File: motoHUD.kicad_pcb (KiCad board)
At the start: 2 copper layers, 128 x 55 mm, 90 parts, among them J1 POWER, J10 LCD Connector, J2 SIGNAL, J3 THERM1, J4 THERM2, J5 HALL, J6 SIG_RPM, J8 USB_B_Mini, J9 STLink, M1 X27 168, Q1 2N7002KQ-13, Q2 2N7002KQ-13, U1 AZ1117-3.3, U2 AZ1117-5.0, U3 LM2903DT, U4 STM32F103C8Tx, U5 M95320-WMN6P, Y1 8M, Y2 32,768k

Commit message: schematic rev2
2nd revision schematic and updated BOM
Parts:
- J10: footprint motoHUD:ILI9341 FFC -> motoHUD:ILI9341FFC
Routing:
- net Net-(J2-Pad2): track 7.66 -> 8.49 mm

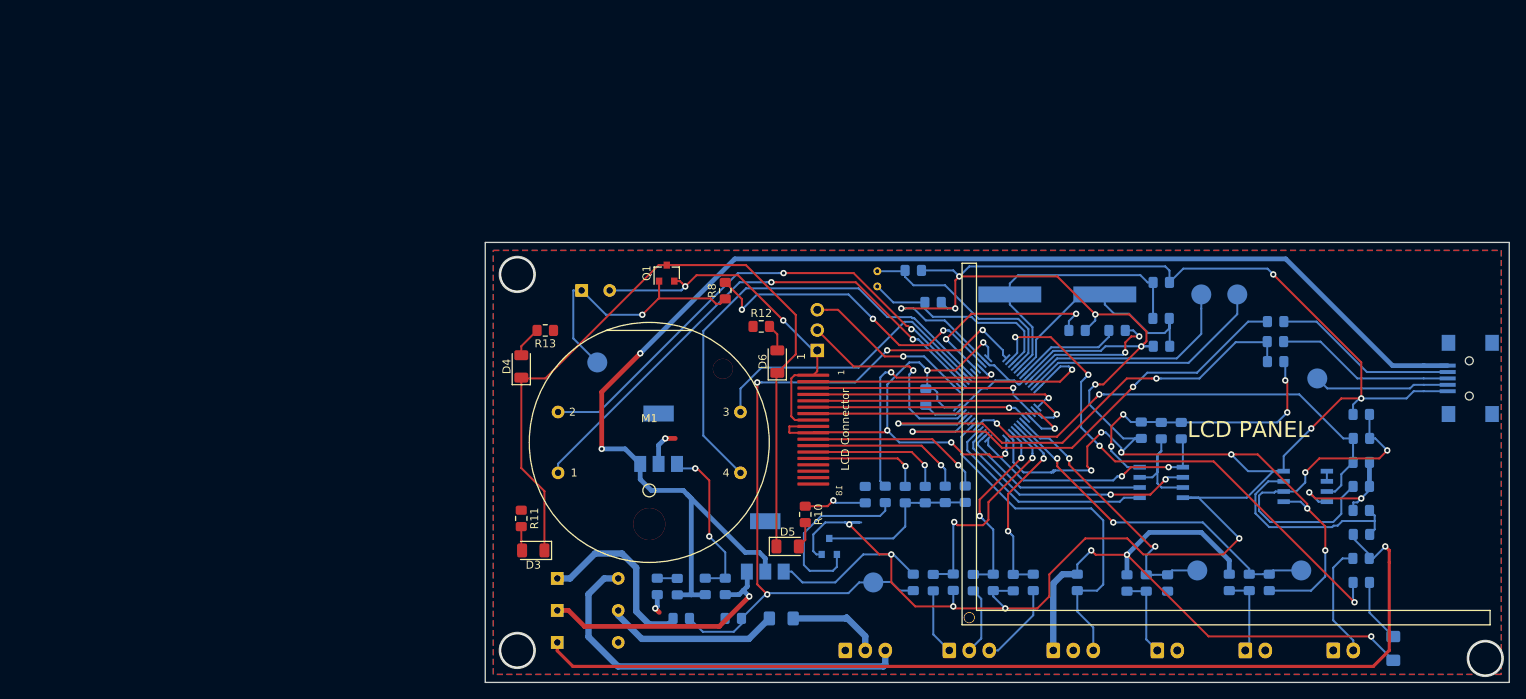
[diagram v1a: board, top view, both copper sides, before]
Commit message: new netlist imported to board design
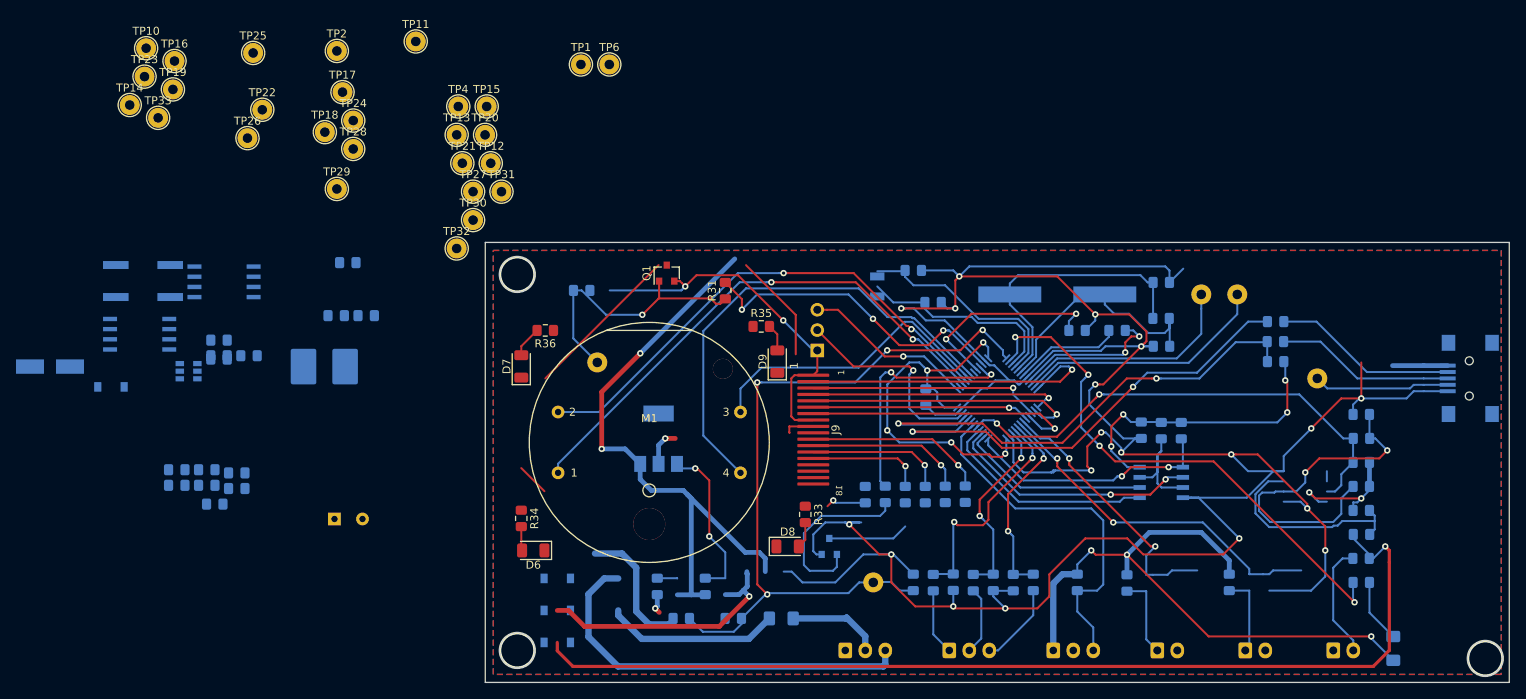
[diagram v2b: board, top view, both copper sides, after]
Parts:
- removed C2: 10u, Capacitor_SMD:C_0805_2012Metric_Pad1.15x1.40mm_HandSolder
- removed C3, C4: 2,2u, Capacitor_SMD:C_0805_2012Metric_Pad1.15x1.40mm_HandSolder
- removed C7: 22u, Capacitor_SMD:C_0805_2012Metric_Pad1.15x1.40mm_HandSolder
- removed C8: 100u, Capacitor_THT:CP_Radial_D8.0mm_P3.50mm
- removed the D8 at (85.0, 131.0)
- removed J10: LCD Connector, motoHUD:ILI9341FFC
- removed R4, R5: 100K, Resistor_SMD:R_0805_2012Metric_Pad1.15x1.40mm_HandSolder
- removed REF**: KiCAD Logo, Symbol:Symbol_KiCAD-Logo_CopperAndSilkScreenTop
- added C12: 10u 16v, Capacitor_SMD:C_0805_2012Metric_Pad1.15x1.40mm_HandSolder, B.Cu at (58.8, 83.5)
- added C13: 0,1u, Capacitor_SMD:C_0805_2012Metric_Pad1.15x1.40mm_HandSolder, B.Cu at (41.2, 111.4)
- added C14: 10u 16v, Capacitor_SMD:C_0805_2012Metric_Pad1.15x1.40mm_HandSolder, B.Cu at (37.4, 109.4)
- added C15: 10u 16v, Capacitor_SMD:C_0805_2012Metric_Pad1.15x1.40mm_HandSolder, B.Cu at (37.4, 111.4)
- added C16: 100u, Capacitor_THT:CP_Radial_D8.0mm_P3.50mm, B.Cu at (57.1, 115.6)
- added C21: 22u, Capacitor_SMD:C_0805_2012Metric_Pad1.15x1.40mm_HandSolder, B.Cu at (88.0, 87.0)
- added C22: 22u, Capacitor_SMD:C_0805_2012Metric_Pad1.15x1.40mm_HandSolder, B.Cu at (57.4, 90.2)
- added C25: 22u, Capacitor_SMD:C_0805_2012Metric_Pad1.15x1.40mm_HandSolder, B.Cu at (44.9, 111.8)
- added D3: 1N4148W-7-F, Diode_SMD:D_SOD-123, B.Cu at (85.0, 131.0)
- added D4: STPS1L40A, Diode_SMD:D_SMA_Handsoldering, B.Cu at (21.6, 96.5)
- added D5: 1N4148W-7-F, Diode_SMD:D_SOD-123, B.Cu at (29.2, 99.1)
- added J9: LCD Connector, motoHUD:ILI9341 FFC, F.Cu at (117.0, 104.4)
- added L1: DLG-0403-220, Inductor_SMD:L_2816_7142Metric_Pad3.20x4.45mm_HandSolder, B.Cu at (55.9, 96.5)
- added R13: 51,1k, Resistor_SMD:R_0805_2012Metric_Pad1.15x1.40mm_HandSolder, B.Cu at (42.7, 95.2)
- added R14: 1,5k, Resistor_SMD:R_0805_2012Metric_Pad1.15x1.40mm_HandSolder, B.Cu at (42.2, 113.7)
- added R15: 10k, Resistor_SMD:R_0805_2012Metric_Pad1.15x1.40mm_HandSolder, B.Cu at (42.7, 93.2)
- added R16: 0R, Resistor_SMD:R_0805_2012Metric_Pad1.15x1.40mm_HandSolder, B.Cu at (41.2, 109.4)
- added R17: 0R, Resistor_SMD:R_0805_2012Metric_Pad1.15x1.40mm_HandSolder, B.Cu at (42.7, 95.6)
- added R26: 2,2k, Resistor_SMD:R_0805_2012Metric_Pad1.15x1.40mm_HandSolder, B.Cu at (46.5, 95.2)
- added R32: 0R, Resistor_SMD:R_0805_2012Metric_Pad1.15x1.40mm_HandSolder, B.Cu at (44.9, 109.8)
- added R62: 0R, Resistor_SMD:R_0805_2012Metric_Pad1.15x1.40mm_HandSolder, B.Cu at (61.1, 90.2)
- added SW1: TACTM-613N-F, Button_Switch_SMD:SW_SPST_EVQQ2, B.Cu at (33.2, 85.8)
- added TP10: TEMP1, TestPoint:TestPoint_THTPad_D2.5mm_Drill1.2mm, F.Cu at (33.6, 56.7)
- added TP11: TEMP2, TestPoint:TestPoint_THTPad_D2.5mm_Drill1.2mm, F.Cu at (67.3, 55.9)
- added TP12: RPMA, TestPoint:TestPoint_THTPad_D2.5mm_Drill1.2mm, F.Cu at (76.7, 71.1)
- added TP13: BOOST, TestPoint:TestPoint_THTPad_D2.5mm_Drill1.2mm, F.Cu at (72.4, 67.6)
- added TP14: BCKL_V, TestPoint:TestPoint_THTPad_D2.5mm_Drill1.2mm, F.Cu at (31.6, 63.8)
- added TP15: RPMC, TestPoint:TestPoint_THTPad_D2.5mm_Drill1.2mm, F.Cu at (76.2, 64.0)
- added TP16: RPMD, TestPoint:TestPoint_THTPad_D2.5mm_Drill1.2mm, F.Cu at (37.2, 58.3)
- added TP17: BLINK, TestPoint:TestPoint_THTPad_D2.5mm_Drill1.2mm, F.Cu at (58.2, 62.2)
- added TP18: BLINK12, TestPoint:TestPoint_THTPad_D2.5mm_Drill1.2mm, F.Cu at (55.9, 67.2)
- added TP19: HIBEAM, TestPoint:TestPoint_THTPad_D2.5mm_Drill1.2mm, F.Cu at (37.0, 61.9)
- added TP20: HIBEAM12, TestPoint:TestPoint_THTPad_D2.5mm_Drill1.2mm, F.Cu at (76.0, 67.6)
- added TP21: NTR, TestPoint:TestPoint_THTPad_D2.5mm_Drill1.2mm, F.Cu at (73.1, 71.1)
- added TP22: NTR12, TestPoint:TestPoint_THTPad_D2.5mm_Drill1.2mm, F.Cu at (48.1, 64.4)
- added TP23: CS2, TestPoint:TestPoint_THTPad_D2.5mm_Drill1.2mm, F.Cu at (33.4, 60.3)
- added TP24: SCK1, TestPoint:TestPoint_THTPad_D2.5mm_Drill1.2mm, F.Cu at (59.5, 65.8)
- added TP25: D/C, TestPoint:TestPoint_THTPad_D2.5mm_Drill1.2mm, F.Cu at (47.0, 57.3)
- added TP26: MOSI1, TestPoint:TestPoint_THTPad_D2.5mm_Drill1.2mm, F.Cu at (46.3, 68.0)
- added TP27: LCDCAP, TestPoint:TestPoint_THTPad_D2.5mm_Drill1.2mm, F.Cu at (74.5, 74.7)
- added TP28: CS1, TestPoint:TestPoint_THTPad_D2.5mm_Drill1.2mm, F.Cu at (59.5, 69.3)
- added TP29: MISO1, TestPoint:TestPoint_THTPad_D2.5mm_Drill1.2mm, F.Cu at (57.4, 74.3)
- added TP30: LCDV, TestPoint:TestPoint_THTPad_D2.5mm_Drill1.2mm, F.Cu at (74.5, 78.2)
- added TP31: SCK2, TestPoint:TestPoint_THTPad_D2.5mm_Drill1.2mm, F.Cu at (78.0, 74.7)
- added TP32: MOSI2, TestPoint:TestPoint_THTPad_D2.5mm_Drill1.2mm, F.Cu at (72.4, 81.8)
- added TP33: MISO2, TestPoint:TestPoint_THTPad_D2.5mm_Drill1.2mm, F.Cu at (35.1, 65.4)
- added TP8: PA1, TestPoint:TestPoint_THTPad_D2.5mm_Drill1.2mm, B.Cu at (170.0, 87.5)
- added TP9: USB_ID, TestPoint:TestPoint_THTPad_D2.5mm_Drill1.2mm, B.Cu at (180.0, 98.0)
- added U5: MCP16301, Package_TO_SOT_SMD:SOT-23-6, B.Cu at (38.9, 97.1)
- C17: renamed from C1; value 10u -> 10u 16v
- D1, D2: value 1N4148 -> 1N4148W-7-F; footprint Diode_THT:D_DO-35_SOD27_P7.62mm_Horizontal -> Diode_SMD:D_SOD-123
- D10: renamed from D7; value STATUS -> LEDSTATUS
- F1: value C1F-375 -> ESKA FUSE 0805-FF PW 0A5; footprint Fuse:Fuse_1206_3216Metric_Pad1.42x1.75mm_HandSolder -> Capacitor_SMD:C_1206_3216Metric_Pad1.42x1.75mm_HandSolder
- J8: renamed from J9; value STLink -> ICSP
- R21: renamed from R3; value 10K -> 10k
- R210: renamed from R39; value 20M -> 1M
- R211: renamed from R9; value 10K -> 10k
- R22: renamed from R1; value 7,6K -> 7,6k
- R23: renamed from R2; value 7,6K -> 7,6k
- R27: renamed from R36; value 100K -> 100k
- R28: renamed from R37; value 100K -> 100k
- R33: renamed from R10; value 4R -> 100R
- R34: renamed from R11; value 4R -> 100R
- R35: renamed from R12; value 4R -> 100R
- R36: renamed from R13; value 4R -> 100R
- R51: renamed from R23; value 10K -> 10k
- R52: renamed from R24; value 10K -> 10k
- R54: renamed from R14; value 100K -> 100k
- R55: renamed from R18; value 10K -> 10k
- R61: renamed from R25; value 1,5K -> 100k
- R63: renamed from R33; value 4R -> 39R
- R64: renamed from R32; value 4R -> 39R
- R65: renamed from R31; value 4R -> 39R
- R66: renamed from R30; value 4R -> 39R
- R73: renamed from R29; value 1,5K -> 1,5k
- R74: renamed from R28; value 510R -> 1,5k
- TP1: value THERM1 -> VEL; footprint TestPoint:TestPoint_Pad_D2.5mm -> TestPoint:TestPoint_THTPad_D2.5mm_Drill1.2mm; moved to F.Cu
- TP2: value THERM2 -> 3v3; footprint TestPoint:TestPoint_Pad_D2.5mm -> TestPoint:TestPoint_THTPad_D2.5mm_Drill1.2mm; moved to F.Cu
- TP3: value VRTC -> V_RTC; footprint TestPoint:TestPoint_Pad_D2.5mm -> TestPoint:TestPoint_THTPad_D2.5mm_Drill1.2mm
- TP4: value BCKL_CAP -> V_IGN; footprint TestPoint:TestPoint_Pad_D2.5mm -> TestPoint:TestPoint_THTPad_D2.5mm_Drill1.2mm; moved to F.Cu
- TP5: value USB_ID -> BCKL_CAP; footprint TestPoint:TestPoint_Pad_D2.5mm -> TestPoint:TestPoint_THTPad_D2.5mm_Drill1.2mm
- TP6: value PA0 -> 5V; footprint TestPoint:TestPoint_Pad_D2.5mm -> TestPoint:TestPoint_THTPad_D2.5mm_Drill1.2mm; moved to F.Cu
- TP7: value PA1 -> PA0; footprint TestPoint:TestPoint_Pad_D2.5mm -> TestPoint:TestPoint_THTPad_D2.5mm_Drill1.2mm
- U2: value AZ1117-5.0 -> LM2904DT; footprint Package_TO_SOT_SMD:SOT-223 -> Package_SO:SO-8_5.3x6.2mm_P1.27mm
- U3: value LM2903DT -> LM2904DT; footprint Package_SO:SOIC-8_3.9x4.9mm_P1.27mm -> Package_SO:SO-8_5.3x6.2mm_P1.27mm
- Y1: value 8M -> HC49USM-FF3F18-8M
- Y2: value 32,768k -> LFXTAL009678; footprint Crystal:Crystal_C26-LF_D2.1mm_L6.5mm_Horizontal -> Crystal:Crystal_SMD_3215-2Pin_3.2x1.5mm
- moved U3 146.9 mm to (32.8, 92.5)
- moved TP2 136.9 mm to (57.4, 57.1)
- moved TP1 99.7 mm to (88.0, 58.8)
- moved TP5 90.0 mm to (90.0, 96.0)
- moved TP6 79.4 mm to (91.5, 58.8)
- moved U2 75.3 mm to (43.3, 85.9), turned to 0 degrees
- moved TP4 36.4 mm to (72.6, 64.0)
- moved TP7 4.50 mm to (165.5, 87.5)
- renumbered C6 to C11, C5 to C18, C15 to C23, C16 to C24, C13 to C30, C12 to C31, C11 to C32, C10 to C33, C14 to C34, D3 to D6, D4 to D7, D5 to D8, D6 to D9, J3 to J2, J4 to J3, J5 to J4, J6 to J5, J2 to J6, J8 to J7, R6 to R11, R7 to R12, R34 to R24, R35 to R25, R38 to R29, R8 to R31, R16 to R41, R17 to R42, R19 to R43, R20 to R44, R21 to R45, R22 to R46, R15 to R53, R27 to R71, R26 to R72, U4 to U1, U1 to U4, U5 to U6
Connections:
- C18 pad 1: +3V3 -> Net-(C18-Pad1)
- D2 pad 2: Net-(D2-Pad2) -> GND
- D6 pad 1: Net-(D3-Pad1) (its old number) -> Net-(D6-Pad1)
- D7 pad 1: Net-(D3-Pad1) (its old number) -> Net-(D6-Pad1)
- D8 pad 1: Net-(D3-Pad1) (its old number) -> Net-(D8-Pad1)
- D9 pad 1: Net-(D3-Pad1) (its old number) -> Net-(D6-Pad1)
- F1 pad 2: Net-(D2-Pad2) -> VCC
- J2 pad 1: Net-(J3-Pad1) -> Net-(J2-Pad1)
- J3 pad 1: Net-(J4-Pad1) -> Net-(J3-Pad1)
- J7 pad 4: Net-(J8-Pad4) -> Net-(J7-Pad4)
- Q1 pad 1: Net-(D3-Pad1) (its old number) -> Net-(D6-Pad1)
- Q1 pad 2: Net-(C8-Pad1) -> Net-(C21-Pad1)
- R210 pad 1: Net-(R37-Pad1) -> Net-(R210-Pad1)
- R22 pad 1: Net-(J3-Pad1) -> Net-(J2-Pad1)
- R23 pad 1: Net-(J4-Pad1) -> Net-(J3-Pad1)
- R25 pad 2: Net-(R35-Pad2) -> Net-(R25-Pad2)
- R27 pad 1: Net-(R35-Pad2) -> Net-(R25-Pad2)
- R28 pad 1: Net-(R37-Pad1) -> Net-(R210-Pad1)
- R29 pad 1: Net-(R37-Pad1) -> Net-(R210-Pad1)
- R31 pad 1: Net-(C8-Pad1) -> Net-(C21-Pad1)
- R33 pad 1: +3V3 -> +5V
- R34 pad 1: +3V3 -> +5V
- R35 pad 1: +3V3 -> +5V
- R36 pad 1: +3V3 -> +5V
- R63 pad 2: Net-(Q2-Pad1) -> Net-(R62-Pad1)
- R64 pad 2: Net-(Q2-Pad1) -> Net-(R62-Pad1)
- R65 pad 2: Net-(Q2-Pad1) -> Net-(R62-Pad1)
- R66 pad 2: Net-(Q2-Pad1) -> Net-(R62-Pad1)
- TP1 pad 1: SIG_TEMP1 -> SIG_VEL
- TP2 pad 1: SIG_TEMP2 -> +3V3
- TP4 pad 1: Net-(C8-Pad1) -> VCC
- TP5 pad 1: Net-(J8-Pad4) -> Net-(C21-Pad1)
- TP6 pad 1: Net-(TP6-Pad1) -> +5V
- U1 pad 10: Net-(TP6-Pad1) -> Net-(TP7-Pad1)
- U1 pad 11: Net-(TP7-Pad1) -> USERIN
- U1 pad 31: Net-(U4-Pad31) -> (no net)
- U1 pad 38: Net-(U4-Pad38) -> (no net)
- U1 pad 43: Net-(U4-Pad43) -> (no net)
- U2 pad 1: GND -> SIG_TEMP1
- U2 pad 2: +5V -> SIG_TEMP1
- U2 pad 3: VCC -> Net-(J2-Pad1)
- U2 pad 4: (no net) -> GND
- U3 pad 1: GND -> SIG_RPM
- U3 pad 2: Net-(R37-Pad1) -> Net-(R25-Pad2)
- U3 pad 3: Net-(R35-Pad2) -> Net-(R210-Pad1)
- U3 pad 5: Net-(U3-Pad5) -> (no net)
- U3 pad 6: Net-(U3-Pad5) -> (no net)
- U3 pad 7: SIG_RPM -> (no net)
- U4 pad 2: +3V3 -> Net-(C18-Pad1)
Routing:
- net Net-(D3-Pad1) (its old number): track 95.5 -> 0.00 mm
- net +5V: track 170.4 -> 82.7 mm
- net Net-(R37-Pad1): track 42.2 -> 0.00 mm, vias 2 -> 0
- net Net-(R210-Pad1): track 0.00 -> 42.2 mm, vias 0 -> 2
- net Net-(D3-Pad1): track 126.3 -> 164.2 mm
- net Net-(C8-Pad1): track 34.1 -> 0.00 mm, vias 1 -> 0
- net Net-(C21-Pad1): track 0.00 -> 34.1 mm, vias 0 -> 1
- net USERIN: track 0.00 -> 31.5 mm
- net Net-(TP6-Pad1): track 28.7 -> 0.00 mm
- net GND: track 484.8 -> 457.7 mm, vias 24 -> 23
- net Net-(R35-Pad2): track 26.1 -> 0.00 mm
- net Net-(R25-Pad2): track 0.00 -> 26.1 mm
- net +3V3: track 232.3 -> 210.2 mm, vias 19 -> 17
- net VCC: track 32.5 -> 54.3 mm
- net Net-(D2-Pad2): track 21.8 -> 0.00 mm
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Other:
- board text added: "motoHUD rev.2 W. Burdecki 2019"
- board text removed: "motoHUD rev.1 W. Burdecki 2019"

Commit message: rev2 layout and footprints updated
routing TODO
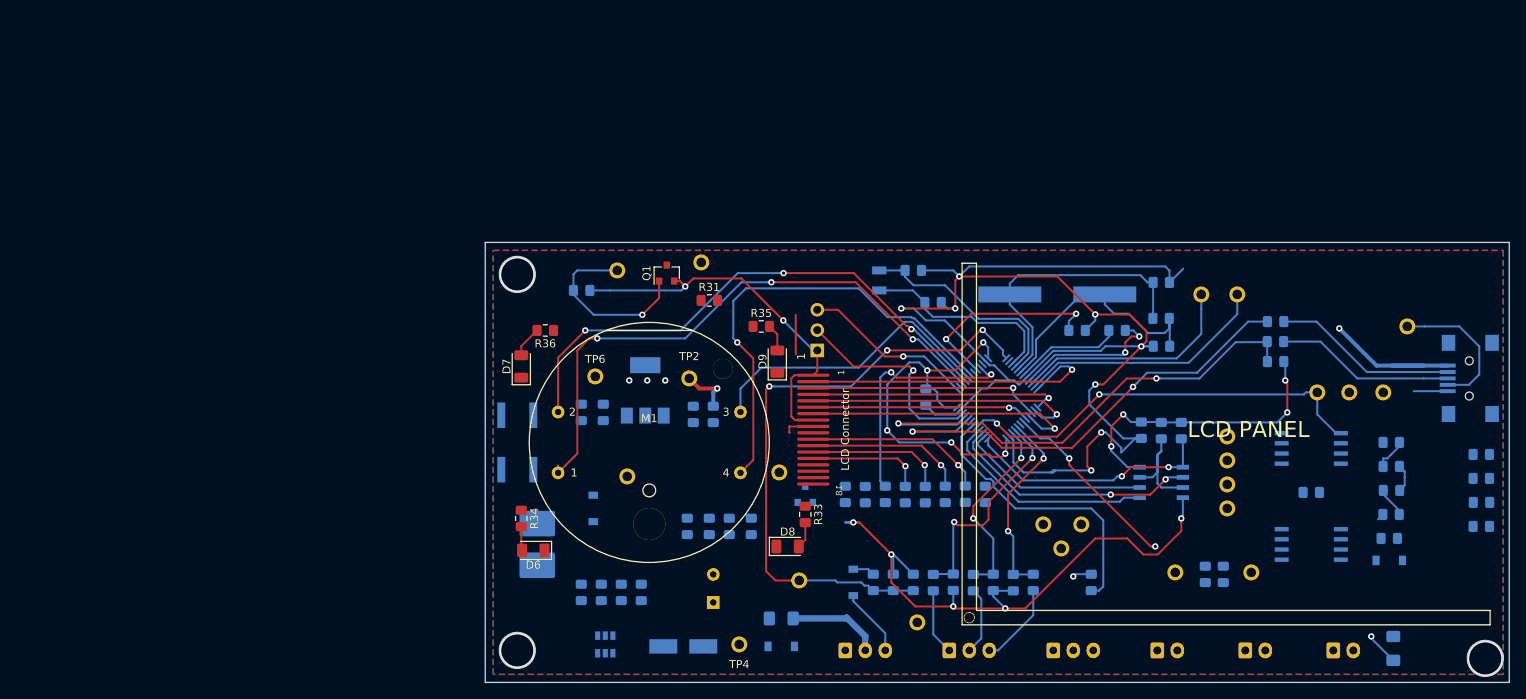
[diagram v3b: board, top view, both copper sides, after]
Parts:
- removed TP17: BLINK, TestPoint:TestPoint_THTPad_D2.5mm_Drill1.2mm
- removed TP18: BLINK12, TestPoint:TestPoint_THTPad_D2.5mm_Drill1.2mm
- removed TP21: NTR, TestPoint:TestPoint_THTPad_D2.5mm_Drill1.2mm
- removed TP22: NTR12, TestPoint:TestPoint_THTPad_D2.5mm_Drill1.2mm
- removed TP24: SCK1, TestPoint:TestPoint_THTPad_D2.5mm_Drill1.2mm
- removed TP25: D/C, TestPoint:TestPoint_THTPad_D2.5mm_Drill1.2mm
- removed TP26: MOSI1, TestPoint:TestPoint_THTPad_D2.5mm_Drill1.2mm
- removed TP28: CS1, TestPoint:TestPoint_THTPad_D2.5mm_Drill1.2mm
- removed TP29: MISO1, TestPoint:TestPoint_THTPad_D2.5mm_Drill1.2mm
- J9: footprint motoHUD:ILI9341 FFC -> motoHUD:ILI9341FFC
- L1: footprint Inductor_SMD:L_2816_7142Metric_Pad3.20x4.45mm_HandSolder -> motoHUD:DLG-0403-220
- SW1: footprint Button_Switch_SMD:SW_SPST_EVQQ2 -> motoHUD:TACTM-613N-F
- TP1, TP10, TP11, TP12, TP13, TP14, TP15, TP16, TP19, TP20, TP23, TP27, TP30, TP31, TP32, TP33: footprint TestPoint:TestPoint_THTPad_D2.5mm_Drill1.2mm -> motoHUD:TestPoint_THTPad_D2.5mm_Drill1.2mm; moved to B.Cu
- TP2, TP3, TP4, TP5, TP6, TP7, TP8, TP9: footprint TestPoint:TestPoint_THTPad_D2.5mm_Drill1.2mm -> motoHUD:TestPoint_THTPad_D2.5mm_Drill1.2mm
- U4: footprint Package_TO_SOT_SMD:SOT-223 -> motoHUD:SOT-223
- moved R26 154.5 mm to (200.5, 107.5)
- moved TP16 148.7 mm to (180.0, 99.8), turned to 90 degrees
- moved U3 147.1 mm to (179.2, 106.8), turned to 180 degrees
- moved TP10 144.4 mm to (162.2, 122.2), turned to 180 degrees
- moved TP23 142.6 mm to (168.8, 105.2)
- moved TP33 140.3 mm to (168.8, 108.2), turned to 180 degrees
- moved U2 139.8 mm to (179.2, 118.8), turned to 180 degrees
- moved C22 123.9 mm to (179.2, 112.2)
- moved TP11 123.7 mm to (171.8, 122.2)
- moved TP15 117.6 mm to (188.2, 99.8), turned to 90 degrees
- moved TP19 114.4 mm to (130.0, 128.5)
- moved TP12 111.1 mm to (184.0, 99.8), turned to 270 degrees
- moved D3 104.5 mm to (189.0, 120.8), turned to 180 degrees
- moved TP32 101.7 mm to (168.8, 114.2), turned to 180 degrees
- moved TP31 97.8 mm to (168.8, 111.2)
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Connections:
- J9 pad 15: (no net) -> Net-(J9-Pad15)
- J9 pad 16: (no net) -> Net-(J9-Pad16)
- J9 pad 17: (no net) -> Net-(J9-Pad17)
- J9 pad 18: (no net) -> Net-(J9-Pad18)
- U1 pad 31: (no net) -> Net-(U1-Pad31)
- U1 pad 38: (no net) -> Net-(U1-Pad38)
- U1 pad 43: (no net) -> Net-(U1-Pad43)
- U3 pad 5: (no net) -> Net-(U3-Pad5)
- U3 pad 6: (no net) -> Net-(U3-Pad6)
- U3 pad 7: (no net) -> Net-(U3-Pad7)
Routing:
- net Net-(D3-Pad1): track 164.2 -> 8.76 mm, vias 1 -> 0
- net GND: track 457.7 -> 304.9 mm, vias 23 -> 15
- net +3V3: track 210.2 -> 126.7 mm
- net STATUS_LED: track 67.4 -> 0.00 mm, vias 4 -> 0
- net +5V: track 82.7 -> 15.5 mm, vias 2 -> 1
- net VCC: track 54.3 -> 0.00 mm, vias 1 -> 0
- net SIG_TEMP2: track 44.0 -> 0.00 mm, vias 2 -> 0
- net Net-(R210-Pad1): track 42.2 -> 0.04 mm, vias 2 -> 0
- net Constant12V: track 50.4 -> 8.51 mm
- net LEDBCKL: track 40.3 -> 0.00 mm, vias 3 -> 0
- net Net-(R25-Pad2): track 26.1 -> 3.53 mm
- net Net-(C25-Pad1): track 22.5 -> 0.00 mm
- net +BATT: track 94.8 -> 77.0 mm, vias 4 -> 3
- net Net-(D1-Pad1): track 17.1 -> 2.76 mm
- net Net-(J5-Pad2): track 14.3 -> 0.88 mm
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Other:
- net class POWER: trace_width 0.25 -> 0.5

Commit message: 2nd button switch added and routed PCB
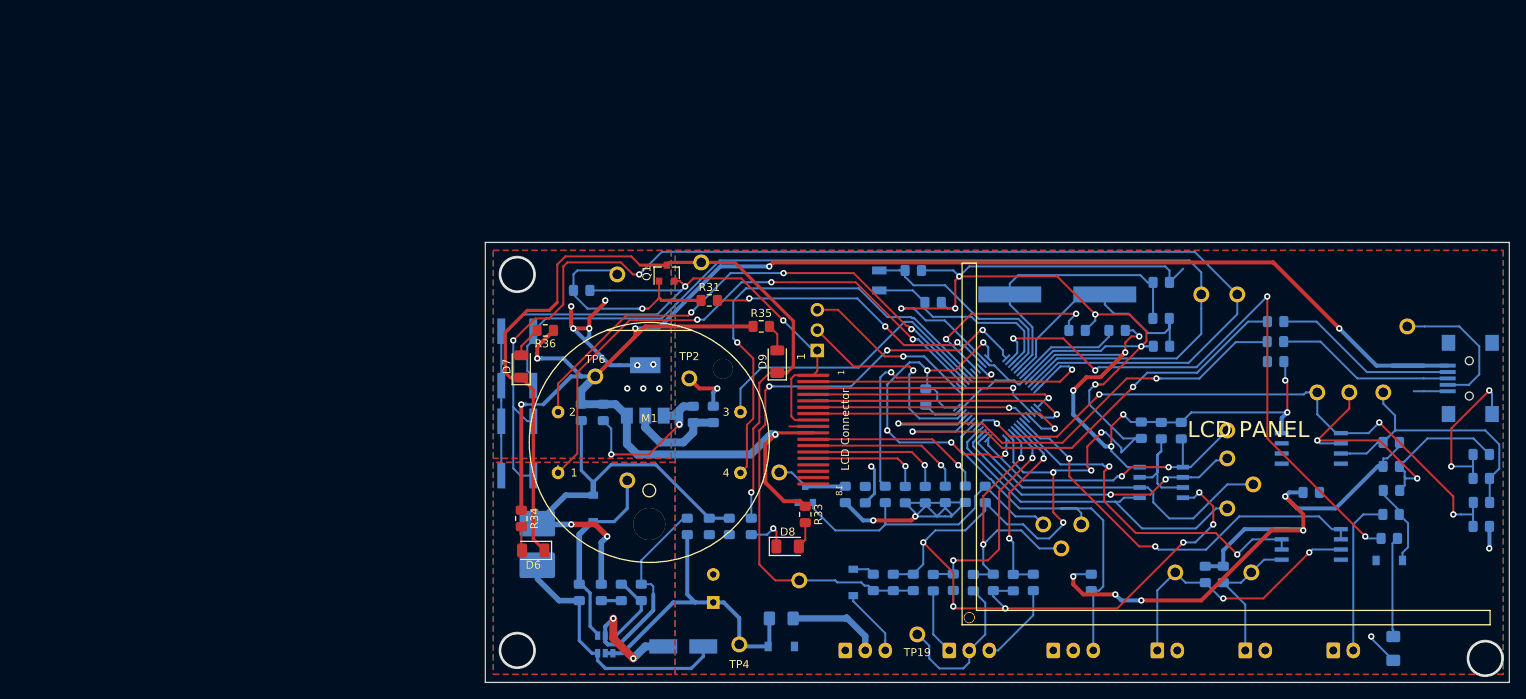
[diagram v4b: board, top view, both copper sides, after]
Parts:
- added SW2: TACTM-613N-F, motoHUD:TACTM-613N-F, B.Cu at (80.0, 95.5)
- TP19: moved to F.Cu
- moved TP31 3.25 mm to (172.0, 111.2)
- moved TP19 1.50 mm to (130.0, 130.0)
- moved SW1 0.75 mm to (80.0, 106.8)
- moved TP23 0.75 mm to (168.8, 104.5)
- moved TP13 0.50 mm to (93.8, 110.8)
- moved TP5 0.50 mm to (92.5, 85.0)
- moved C13 0.25 mm to (87.8, 124.8), turned to 270 degrees
- moved TP33 0.25 mm to (168.8, 108.0)
- turned C17 to 270 degrees
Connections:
- net Net-(TP7-Pad1) renamed USERIN2
- net USERIN renamed USERIN1
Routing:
- net +5V: track 15.5 -> 220.4 mm, vias 1 -> 6
- net GND: track 304.9 -> 449.3 mm, vias 15 -> 24
- net USERIN1: track 31.5 -> 156.8 mm, vias 0 -> 2
- net Net-(D6-Pad1): track 0.00 -> 104.5 mm, vias 0 -> 1
- net +3V3: track 126.7 -> 226.8 mm, vias 17 -> 21
- net USERIN2: track 28.7 -> 126.7 mm
- net STATUS_LED: track 0.00 -> 78.2 mm, vias 0 -> 4
- net Net-(C14-Pad1): track 0.00 -> 54.8 mm, vias 0 -> 2
- net SIG_TEMP2: track 0.00 -> 44.9 mm, vias 0 -> 2
- net Net-(R25-Pad2): track 3.53 -> 43.9 mm, vias 0 -> 2
- net VCC: track 0.00 -> 39.6 mm
- net Net-(C25-Pad1): track 0.00 -> 38.5 mm
- net LEDBCKL: track 0.00 -> 36.9 mm, vias 0 -> 3
- net Net-(J2-Pad1): track 0.00 -> 35.3 mm, vias 0 -> 2
- net Net-(R210-Pad1): track 0.04 -> 34.9 mm
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- added copper zone on B.Cu, net Net-(C18-Pad1)
- added copper zone on F.Cu, net Net-(C18-Pad1)

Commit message: pcb design improvements
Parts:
- D10: value LEDSTATUS -> STATUS
- TP4: moved to B.Cu
- moved TP5 1.12 mm to (91.5, 84.5)
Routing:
- net +3V3: track 226.8 -> 232.7 mm
- net GND: track 449.3 -> 454.5 mm
- net Net-(J9-Pad14): track 14.5 -> 17.5 mm
- net Net-(J9-Pad13): track 17.3 -> 20.3 mm
- net Net-(J9-Pad12): track 19.8 -> 22.8 mm
- net Net-(J9-Pad11): track 22.4 -> 25.4 mm
- net SIG_BLINK: track 28.1 -> 30.9 mm
- net LCD_SCK: track 29.1 -> 31.8 mm
- net LCD_MOSI: track 27.2 -> 29.9 mm
- net LCD_MISO: track 34.9 -> 37.6 mm
- net LCD_DC: track 31.5 -> 34.2 mm
- net LCD_CS: track 34.5 -> 37.2 mm
- net LCD_RESET: track 38.7 -> 41.1 mm
- net Net-(R25-Pad2): track 43.9 -> 42.9 mm
- net Net-(C21-Pad1): track 27.2 -> 26.2 mm
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
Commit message: PCB design improvements
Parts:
- D10: value STATUS -> LEDSTATUS
- TP1, TP10, TP11, TP12, TP13, TP14, TP15, TP16, TP19, TP20, TP23, TP27, TP3, TP30, TP31, TP32, TP33, TP4, TP5, TP7, TP8, TP9: footprint motoHUD:TestPoint_THTPad_D2.5mm_Drill1.2mm -> motoHUD:TestPoint_THTPad_D2.0mm_Drill1.0mm
- TP2, TP6: footprint motoHUD:TestPoint_THTPad_D2.5mm_Drill1.2mm -> motoHUD:TestPoint_THTPad_D2.0mm_Drill1.0mm; moved to B.Cu
- moved TP8 1.02 mm to (169.0, 87.3)
- moved TP13 0.95 mm to (93.8, 111.7)
- moved TP14 0.51 mm to (102.5, 83.6)
- moved C13 0.50 mm to (87.2, 124.8)
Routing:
- net GND: track 454.5 -> 450.2 mm
- net Net-(R54-Pad1): track 25.5 -> 22.3 mm
- net +3V3: track 232.7 -> 234.5 mm
- net USERIN1: track 157.4 -> 156.2 mm
- net SIG_RPM: track 78.9 -> 79.9 mm
- net Net-(C13-Pad1): track 24.9 -> 24.1 mm
- net Net-(C32-Pad1): track 31.6 -> 32.3 mm
- net Net-(C18-Pad1): track 34.3 -> 35.0 mm, vias 9 -> 11
- net Net-(R62-Pad1): track 34.6 -> 35.2 mm
- net +BATT: track 77.7 -> 78.3 mm
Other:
- board text added: "CLK"
- board text added: "GND"
- board text added: "IO"
- board text added: "W. Burdecki 2019"
- board text added: "motoHUD"
- board text added: "rev.2"
- board text removed: "motoHUD rev.2 W. Burdecki 2019"
